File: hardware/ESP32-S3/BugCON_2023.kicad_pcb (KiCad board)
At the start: 2 copper layers, 122.4 x 97.9 mm, 42 parts, among them J1 Conn_01x04_Pin, J2 Conn_01x04_Pin, J3 Conn_01x02, J4 Conn_01x01_Pin, J5 Conn_01x01_Pin, P1 USB_C_Plug_USB2.0, Q1 DMG3415U-7, SW1 RESET, SW2 GPIO, SW3 ON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

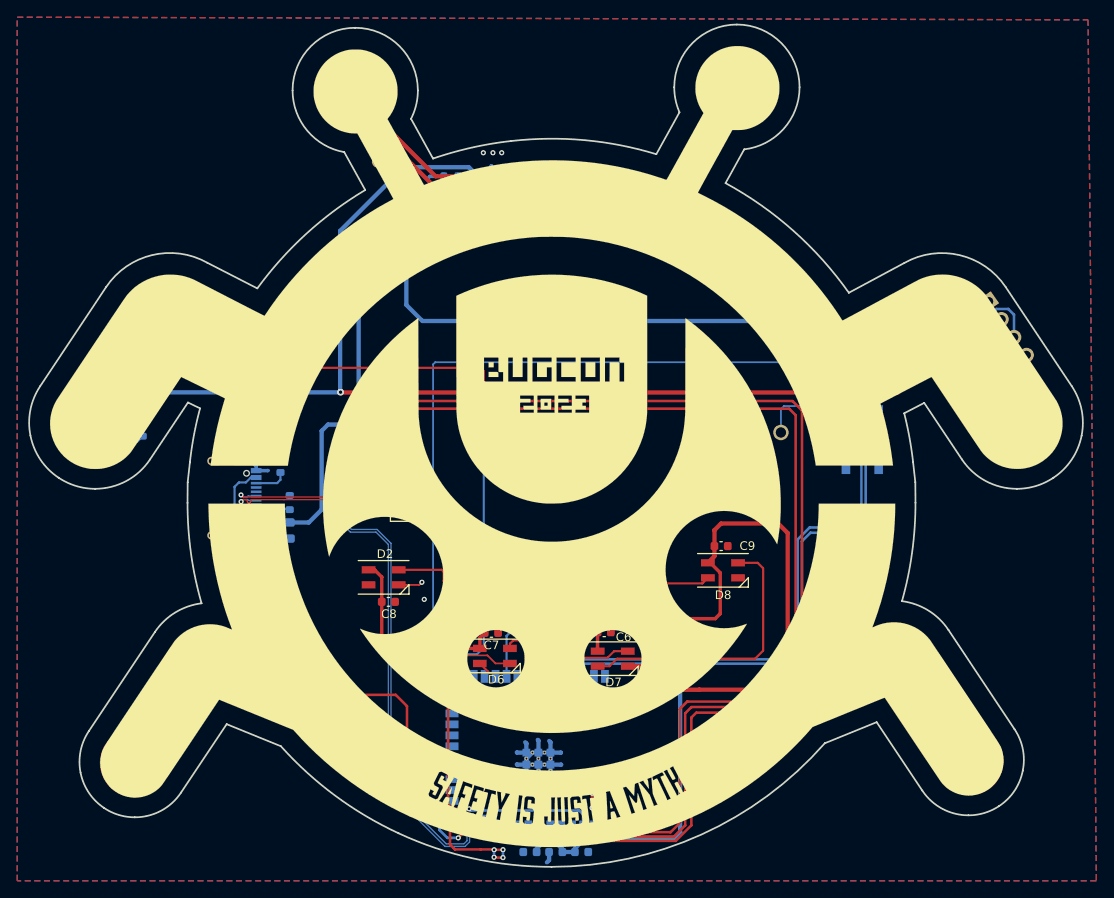
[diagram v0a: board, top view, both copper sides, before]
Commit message: Move_ESP32S3
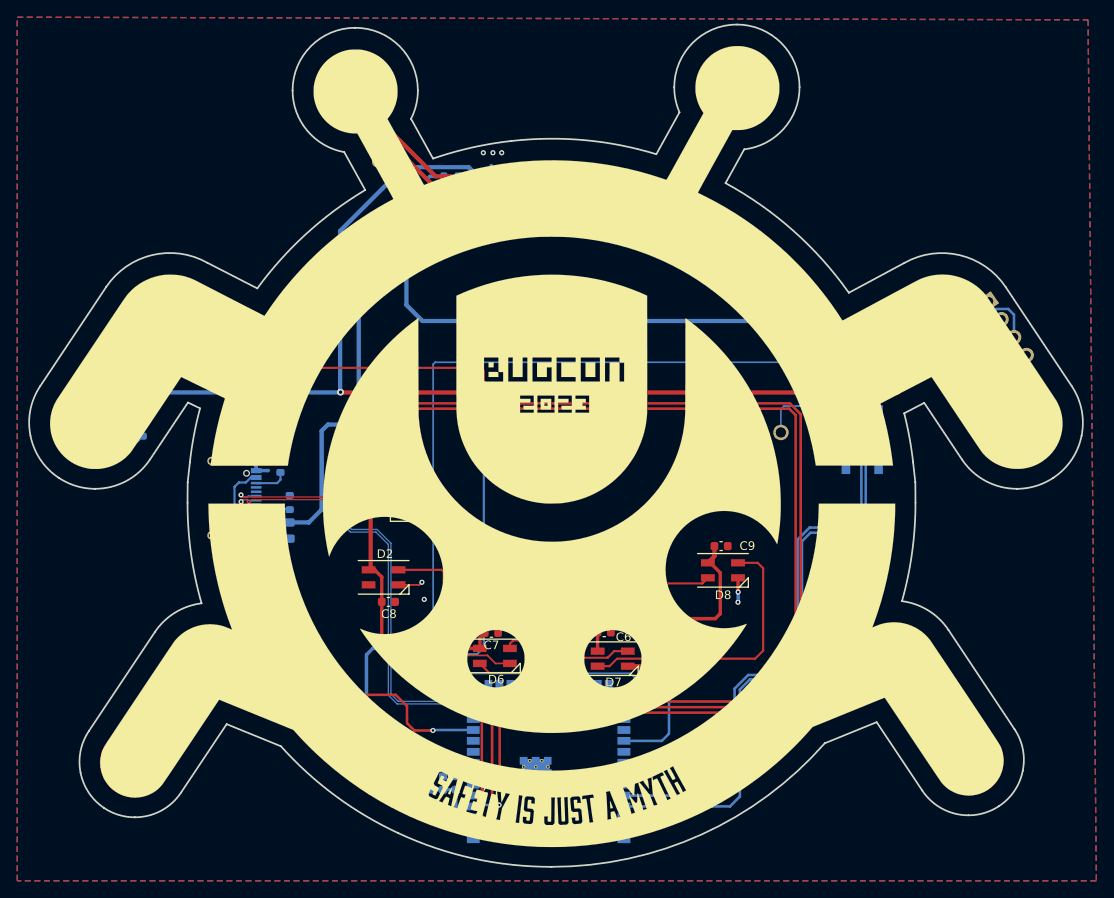
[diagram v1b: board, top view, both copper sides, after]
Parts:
- moved C2 16.7 mm to (132.4, 112.1), turned to 90 degrees
- moved C1 15.4 mm to (130.9, 112.1), turned to 90 degrees
- moved C3 14.1 mm to (129.4, 112.1), turned to 90 degrees
- moved U1 5.07 mm to (143.2, 113.4), turned to 0 degrees
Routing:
- net +3V3: track 304.3 -> 271.9 mm
- net /BOOT: track 99.2 -> 123.0 mm
- net /SDA: track 141.9 -> 119.8 mm
- net /PIN: track 13.5 -> 30.5 mm
- net /D-: track 68.9 -> 54.1 mm
- net /D+: track 68.8 -> 54.5 mm
- net /TCH2: track 60.9 -> 47.2 mm
- net /RST: track 133.3 -> 120.8 mm
- net /TX: track 85.3 -> 93.7 mm
- net /TCH1: track 82.0 -> 75.1 mm
- net /SCL: track 134.5 -> 141.1 mm
- net /RX: track 91.2 -> 97.2 mm
- net GND: track 104.5 -> 98.9 mm, vias 29 -> 22

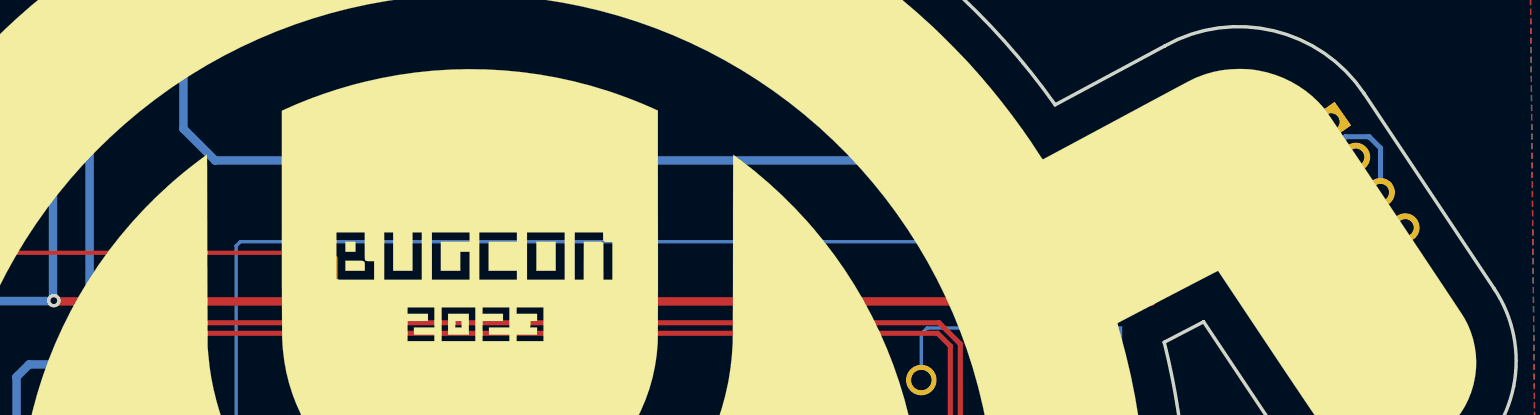
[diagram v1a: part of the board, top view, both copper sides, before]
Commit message: remove 3.3v on Serial connector on esp32s3
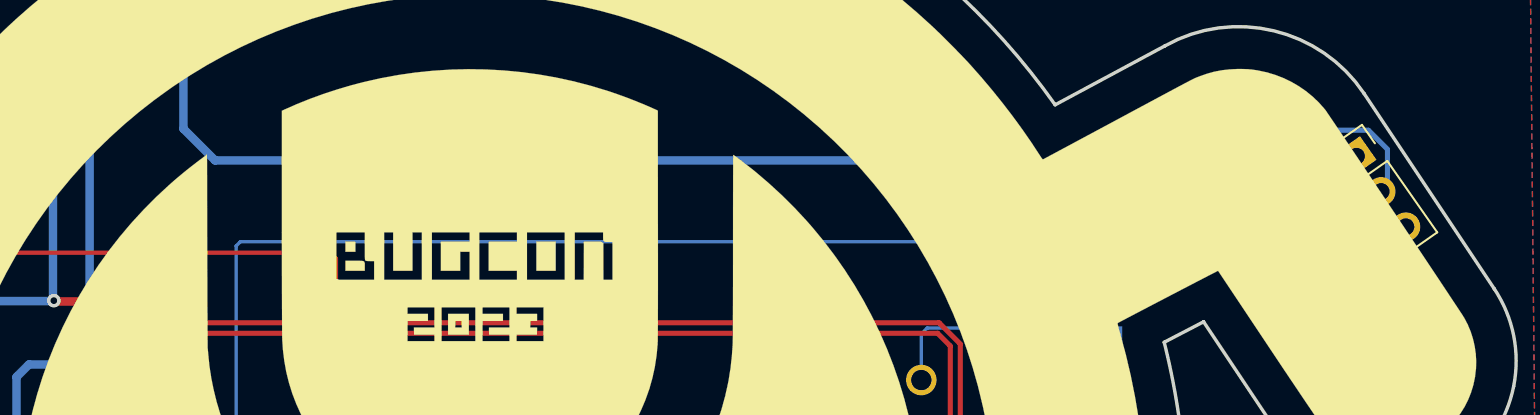
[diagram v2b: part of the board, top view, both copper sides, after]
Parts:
- removed J2: Conn_01x04_Pin, Connector_PinSocket_2.54mm:PinSocket_1x04_P2.54mm_Vertical
- removed kibuzzard-652D8C83: G***, kibuzzard-652D8C83
- added J6: SERIAL, Connector_PinSocket_2.54mm:PinSocket_1x03_P2.54mm_Vertical, F.Cu at (195.8, 58.2)
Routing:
- net +3V3: track 271.9 -> 194.6 mm
- net /RX: track 97.2 -> 98.0 mm

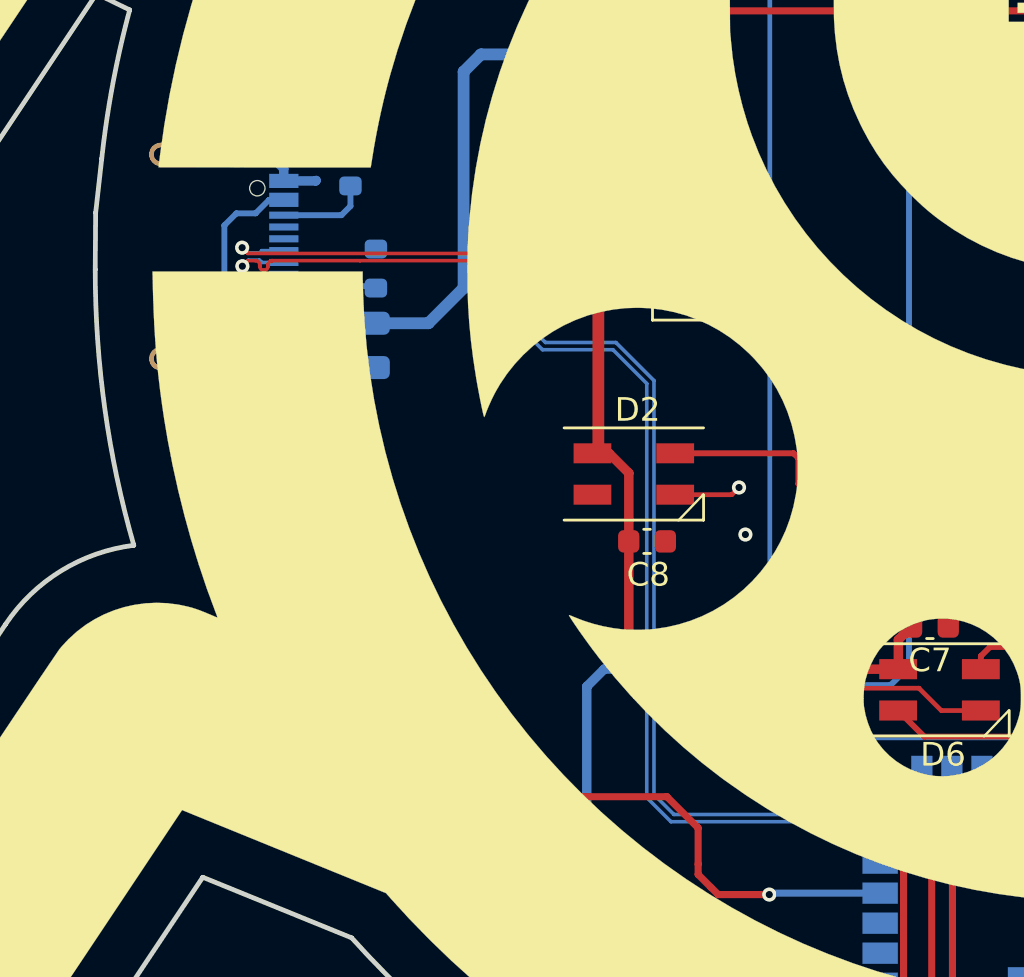
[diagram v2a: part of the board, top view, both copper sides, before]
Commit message: Change_footprint_USBC
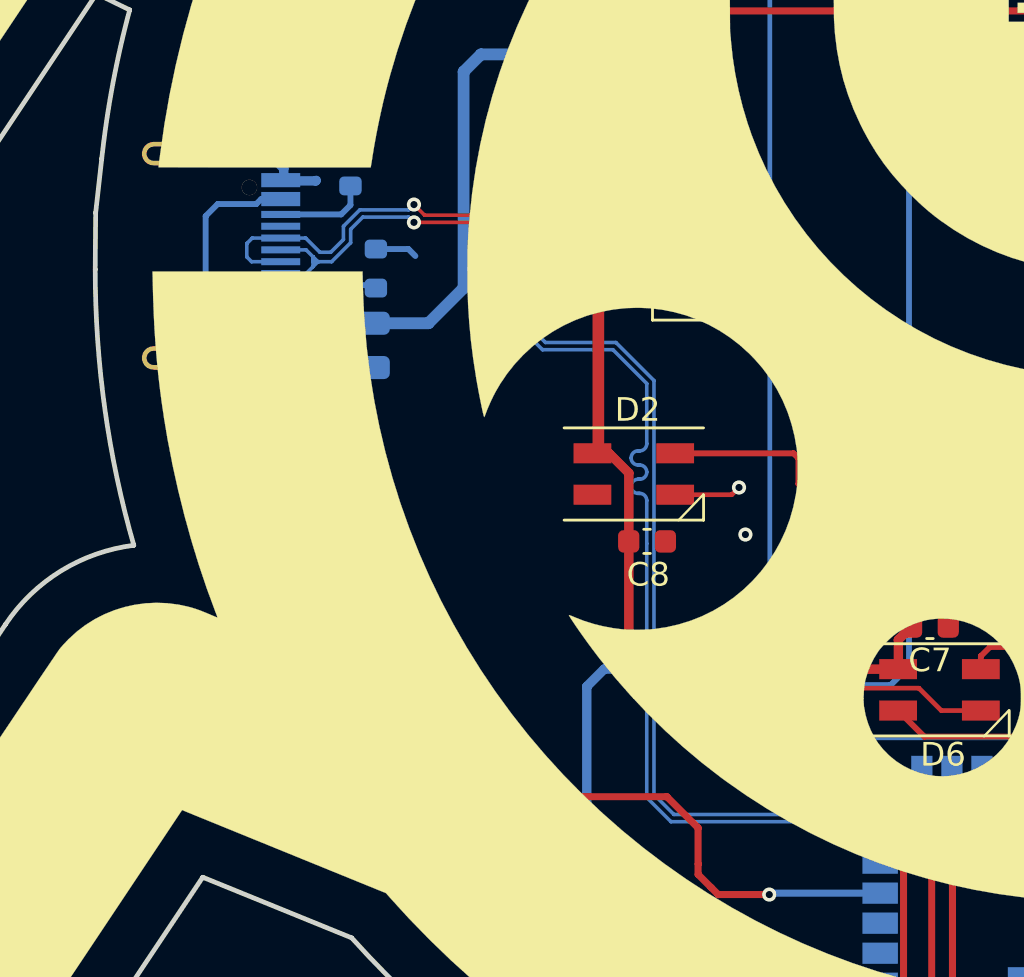
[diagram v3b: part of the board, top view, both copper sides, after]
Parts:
- P1: footprint Connector_USB:USB_C_Receptacle_G-Switch_GT-USB-7010ASV -> FootprintsB:C393939
- moved P1 2.77 mm to (108.2, 79.0)
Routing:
- net Net-(F1-Pad1): track 14.3 -> 15.7 mm
- net /D-: track 54.1 -> 54.8 mm

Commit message: add logo version speaker
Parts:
- added G***: LOGO, ElectronicCats:electronic_cats_logo_8x6, B.Cu at (163.8, 106.7)
- added REF**: KiCad-Logo2_5mm_SilkScreen, Symbol:KiCad-Logo2_5mm_SilkScreen, B.Cu at (124.5, 105.4)
- added kibuzzard-652EA30A: G***, kibuzzard-652EA30A, B.Cu at (177.8, 90.2)
- added kibuzzard-652EA32D: G***, kibuzzard-652EA32D, F.Cu at (120.7, 27.9)
- added kibuzzard-652EA350: G***, kibuzzard-652EA350, B.Cu at (127.3, 38.9)
- added kibuzzard-652EA37F: G***, kibuzzard-652EA37F, B.Cu at (90.9, 66.3)
- added kibuzzard-652EA3B8: G***, kibuzzard-652EA3B8, B.Cu at (179.3, 66.3)
- added kibuzzard-652EA51A: G***, kibuzzard-652EA51A, B.Cu at (101.9, 62.5)
- added kibuzzard-652EA56E: G***, kibuzzard-652EA56E, B.Cu at (95.2, 109.8)
- added kibuzzard-652EA580: G***, kibuzzard-652EA580, B.Cu at (191.8, 109.4)
- added kibuzzard-652EA5CF: G***, kibuzzard-652EA5CF, B.Cu at (101.9, 59.2)
- added kibuzzard-652EA5F7: G***, kibuzzard-652EA5F7, B.Cu at (121.2, 29.0)

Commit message: add more logos
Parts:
- moved kibuzzard-652EA30A 3.07 mm to (180.6, 91.4)
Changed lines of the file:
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@@
   )
   (footprint "kibuzzard-652EA30A" (layer "B.Cu")
-    (at 177.8 90.17 -90)
+    (at 180.594 91.44 -90)
     (descr "Generated with KiBuzzard")
     (tags "kb_params=eyJBbGlnbm1lbnRDaG9pY2UiOiAiQ2VudGVyIiwgIkNhcExlZnRDaG9pY2UiOiAiWyIsICJDYXBSaWdodENob2ljZSI6ICJdIiwgIkZvbnRDb21ib0JveCI6ICJtcGx1cy0xbW4tbWVkaXVtIiwgIkhlaWdodEN0cmwiOiAiMS41IiwgIkxheWVyQ29tYm9Cb3giOiAiRi5TaWxrUyIsICJNdWx0aUxpbmVUZXh0IjogIlNhZmV0eSBpcyBqdXN0IGEgbXl0aCIsICJQYWRkaW5nQm90dG9tQ3RybCI6ICI1IiwgIlBhZGRpbmdMZWZ0Q3RybCI6ICI1IiwgIlBhZGRpbmdSaWdodEN0cmwiOiAiNSIsICJQYWRkaW5nVG9wQ3RybCI6ICI1IiwgIldpZHRoQ3RybCI6ICIifQ==")

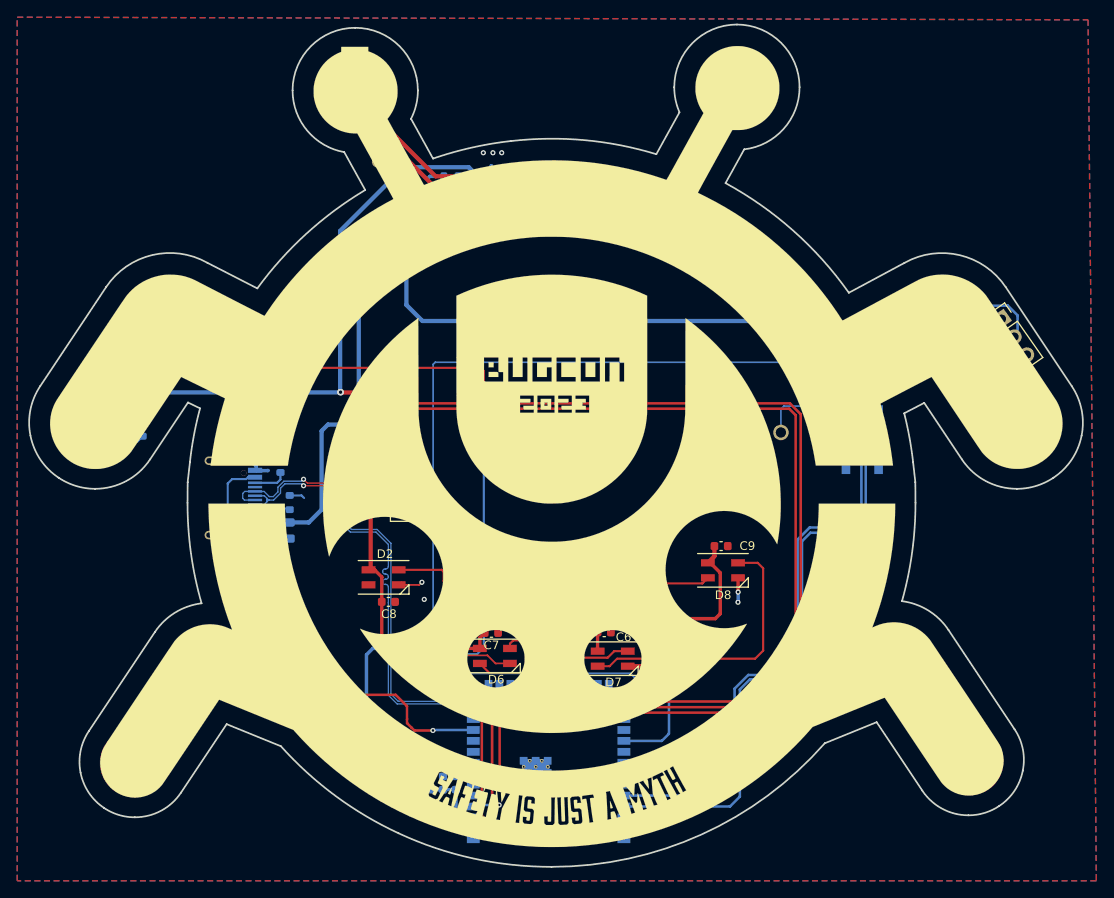
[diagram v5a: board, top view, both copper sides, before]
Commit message: Change_LED´s_Change_Touch_Pad
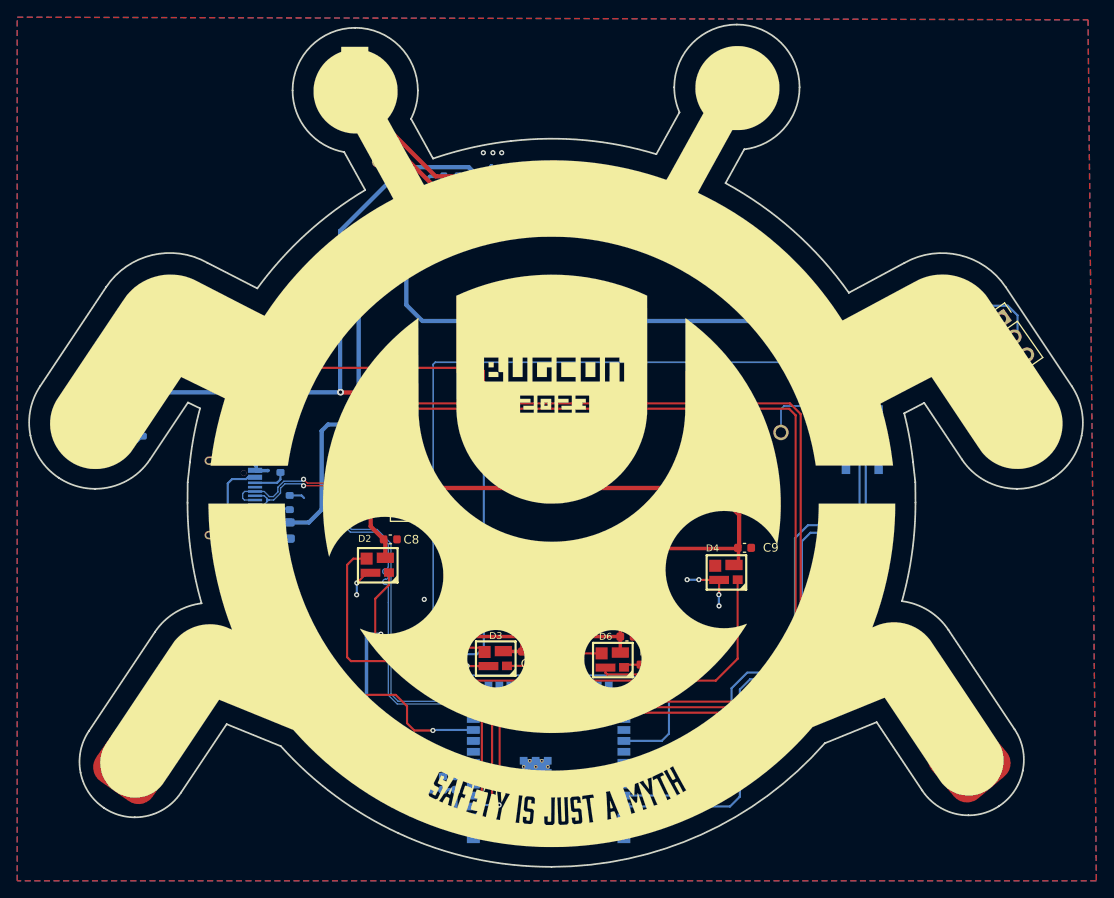
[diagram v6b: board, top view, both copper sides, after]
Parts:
- removed D7, D8: WS2812B, FootprintsB:LED_SK6812MINI_PLCC4_3.5x3.5mm_P1.75mm
- added D3: WS2812B_Mini_X2, FootprintsB:LED-SMD_4P-L3.5-W3.5-TL_WS2812B-1, F.Cu at (137.0, 97.6)
- added D4: WS2812B_Mini_X2, FootprintsB:LED-SMD_4P-L3.5-W3.5-TL_WS2812B-1, F.Cu at (163.8, 87.6)
- D2, D6: value WS2812B -> WS2812B_Mini_X2; footprint FootprintsB:LED_SK6812MINI_PLCC4_3.5x3.5mm_P1.75mm -> FootprintsB:LED-SMD_4P-L3.5-W3.5-TL_WS2812B-1
- moved D6 13.7 mm to (150.6, 97.8)
- moved R9 10.5 mm to (154.6, 98.3)
- moved C8 7.26 mm to (124.8, 83.8)
- moved C7 4.83 mm to (140.8, 96.8)
- moved C9 2.73 mm to (165.9, 84.8)
- moved C6 2.69 mm to (152.3, 95.1)
- moved D2 1.56 mm to (123.3, 86.8)
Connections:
- D2 pad 1: +3V3 -> Net-(D2-DIN)
- D2 pad 2: unconnected-(D2-DOUT-Pad2) -> +3V3
- D2 pad 3: GND -> Net-(D2-DOUT)
- D2 pad 4: Net-(D2-DIN) -> GND
- D6 pad 1: +3V3 -> Net-(D6-DIN)
- D6 pad 2: Net-(D6-DOUT) -> +3V3
- D6 pad 3: GND -> Net-(D3-DIN)
- D6 pad 4: Net-(D6-DIN) -> GND
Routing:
- net Net-(D2-DOUT): track 0.00 -> 71.0 mm
- net +3V3: track 194.6 -> 234.9 mm
- net Net-(D7-DOUT): track 32.7 -> 0.00 mm
- net Net-(D6-DOUT): track 18.7 -> 0.00 mm
- net Net-(D2-DIN): track 37.5 -> 22.0 mm
- net /PIN: track 30.5 -> 15.2 mm
- net Net-(D3-DIN): track 0.00 -> 11.6 mm
- net GND: track 99.3 -> 107.2 mm, vias 22 -> 28
- net Net-(D6-DIN): track 6.30 -> 1.99 mm
- net /RX: track 98.0 -> 101.6 mm
- net /RST: track 120.8 -> 124.3 mm
- net /TX: track 93.7 -> 96.6 mm
- net /TCH2: track 47.2 -> 45.6 mm
- net /TCH1: track 75.1 -> 74.2 mm

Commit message: Change_Neopixels
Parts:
- removed D4: WS2812B_Mini_X2, FootprintsB:LED-SMD_4P-L3.5-W3.5-TL_WS2812B-1
- added D5: WS2812B, FootprintsB:LED-SMD_4P-L3.5-W3.5-TL_WS2812B, F.Cu at (150.6, 97.6)
- D2, D3, D6: value WS2812B_Mini_X2 -> WS2812B; footprint FootprintsB:LED-SMD_4P-L3.5-W3.5-TL_WS2812B-1 -> FootprintsB:LED-SMD_4P-L3.5-W3.5-TL_WS2812B
- moved D3 28.6 mm to (163.6, 87.1)
- moved D6 13.6 mm to (137.0, 97.6)
- moved C8 7.33 mm to (125.6, 91.1), turned to 90 degrees
- moved C9 7.08 mm to (159.2, 87.0), turned to 90 degrees
- moved J6 5.92 mm to (191.5, 62.2)
- moved kibuzzard-652D8C8F 5.66 mm to (188.6, 64.4)
- moved kibuzzard-652D8CA2 5.66 mm to (190.2, 66.5)
- moved kibuzzard-6515D795 5.66 mm to (191.7, 68.4)
- moved C7 4.96 mm to (136.3, 94.9)
- moved C6 2.32 mm to (149.9, 95.0)
- moved R9 1.71 mm to (155.3, 96.8)
- moved D2 0.74 mm to (124.0, 87.0), turned to 180 degrees
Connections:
- D2 pad 1: Net-(D2-DIN) -> +3V3
- D2 pad 2: +3V3 -> Net-(D2-DOUT)
- D2 pad 3: Net-(D2-DOUT) -> GND
- D2 pad 4: GND -> Net-(D2-DIN)
- D3 pad 1: Net-(D3-DIN) -> +3V3
- D3 pad 2: +3V3 -> unconnected-(D3-DOUT-Pad2)
- D3 pad 3: Net-(D2-DIN) -> GND
- D3 pad 4: GND -> Net-(D2-DOUT)
- D6 pad 1: Net-(D6-DIN) -> +3V3
- D6 pad 2: +3V3 -> Net-(D2-DIN)
- D6 pad 3: Net-(D3-DIN) -> GND
- D6 pad 4: GND -> Net-(D5-DOUT)
- R9 pad 2: Net-(D6-DIN) -> Net-(D5-DIN)
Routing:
- net +3V3: track 234.9 -> 200.8 mm
- net GND: track 107.2 -> 84.8 mm, vias 28 -> 24
- net Net-(D2-DOUT): track 71.0 -> 50.1 mm, vias 0 -> 2
- net Net-(D3-DIN): track 11.6 -> 0.00 mm
- net Net-(D5-DOUT): track 0.00 -> 11.0 mm
- net /RST: track 124.3 -> 121.5 mm
- net Net-(D5-DIN): track 0.00 -> 2.19 mm
- net Net-(D6-DIN): track 1.99 -> 0.00 mm
- net /PIN: track 15.2 -> 16.8 mm
- net /BOOT: track 123.0 -> 122.1 mm
